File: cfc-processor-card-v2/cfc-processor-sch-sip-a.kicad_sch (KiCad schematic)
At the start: 27 parts, among them J4 Conn_01x04, Q6 MMBT2907, U7 OSD3358-1G-ISM, U8 SN74AUC1G07DCKR, U9 TLVH431

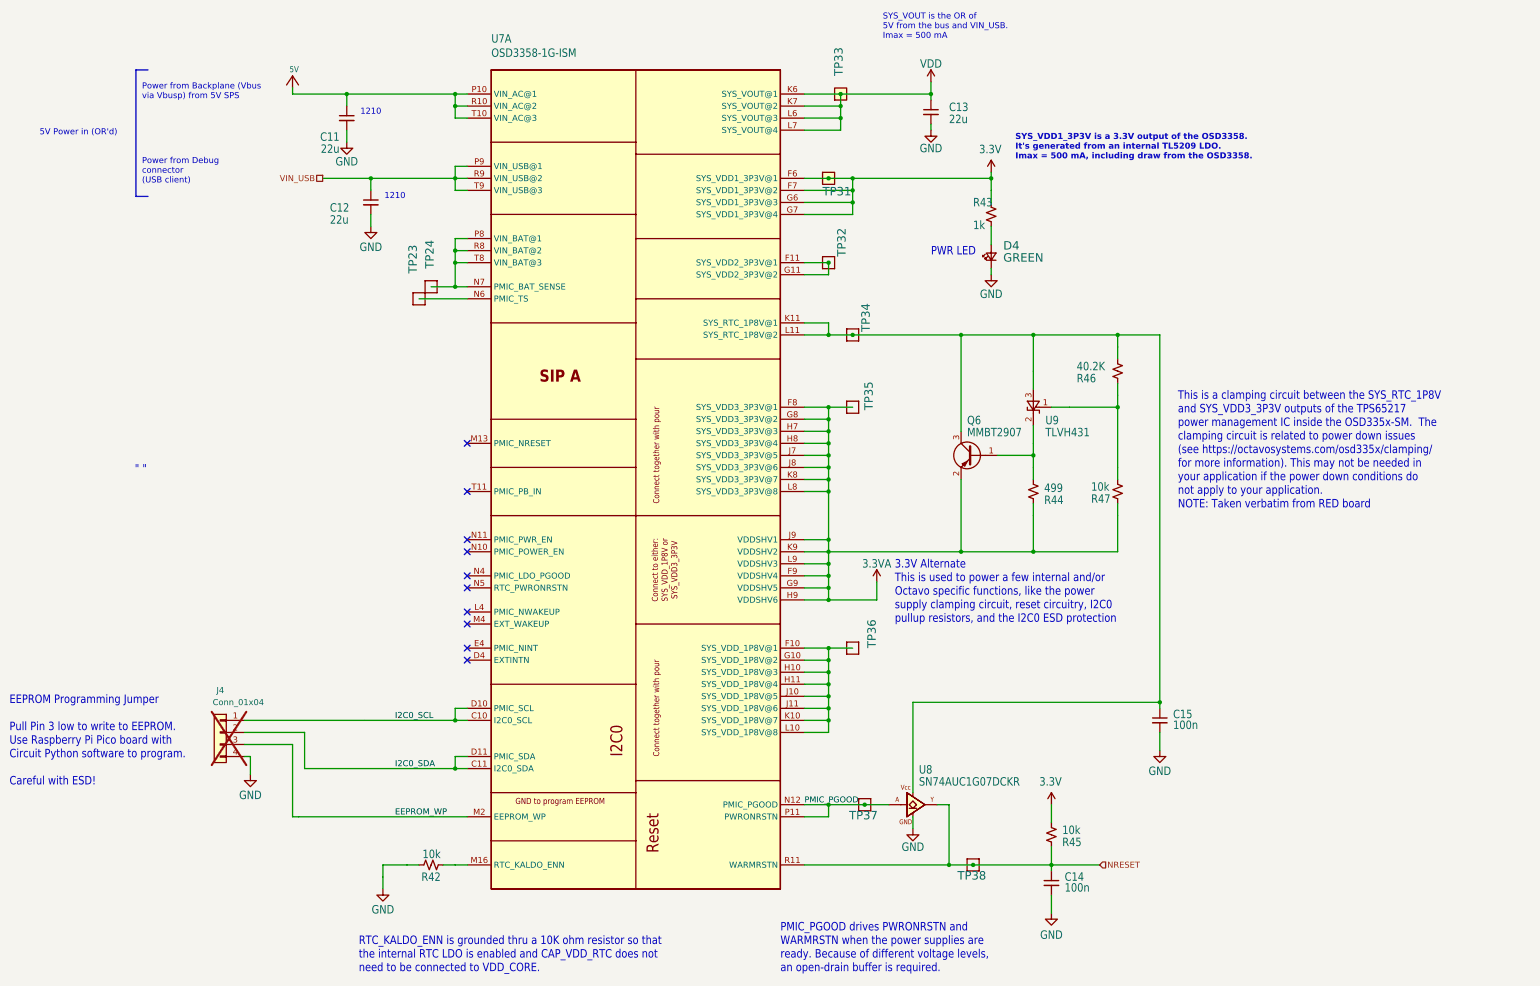
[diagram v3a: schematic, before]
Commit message: Update
Fixed a couple of library issues on testpoints and other misc components. Added Pull up resistors to 8 channel i2c ic
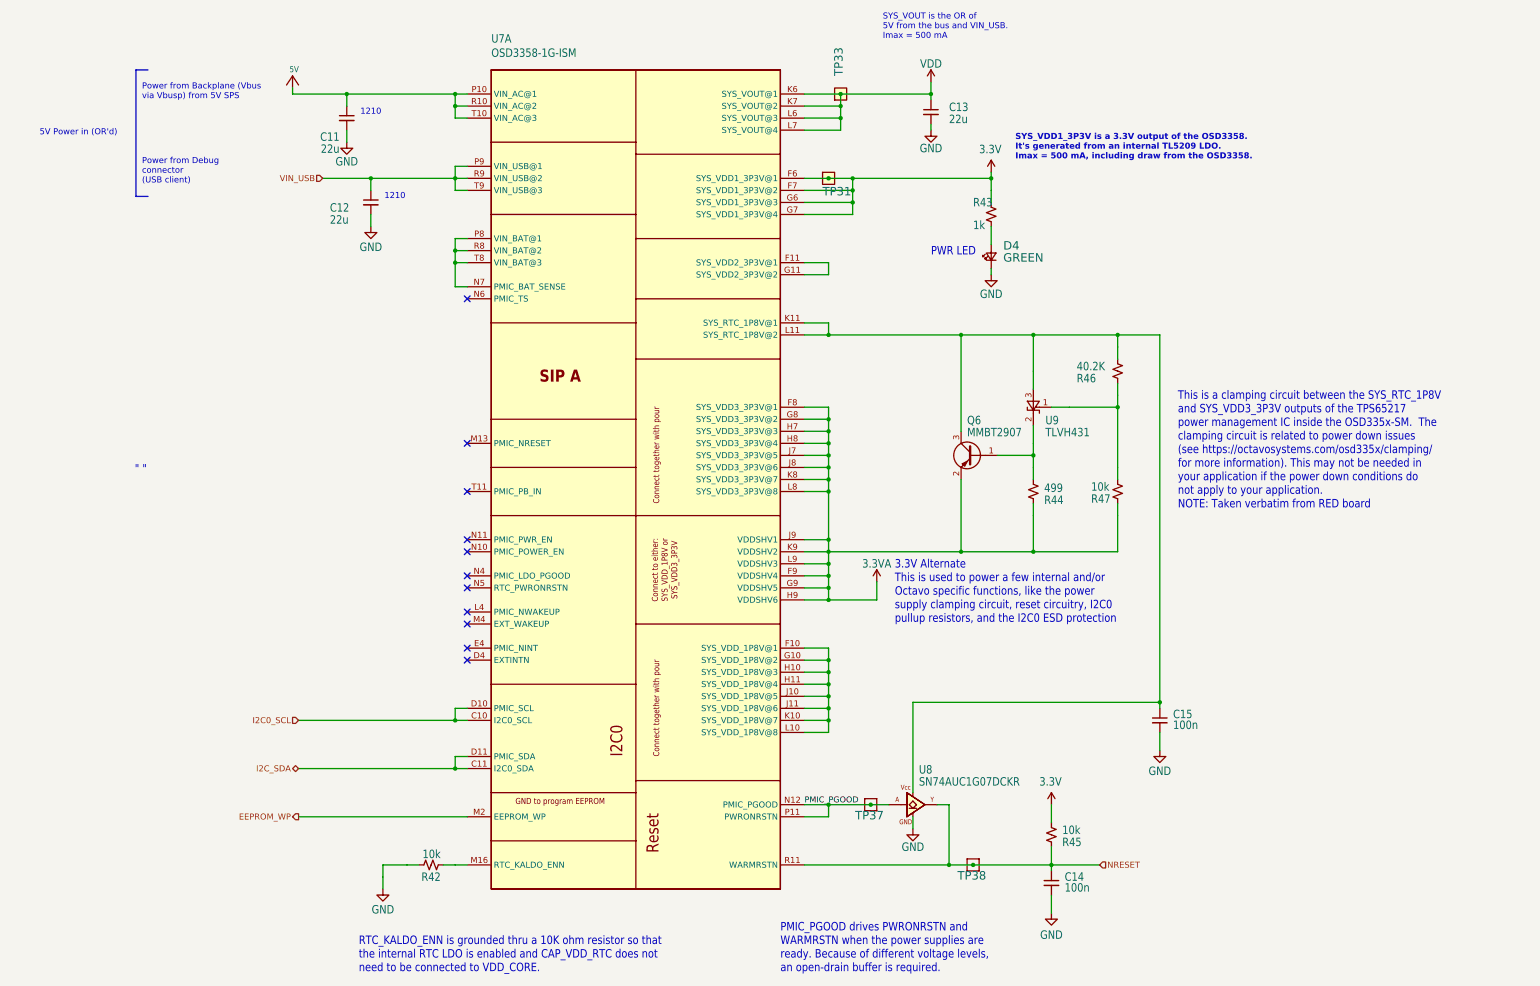
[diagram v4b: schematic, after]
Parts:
- removed J4: Conn_01x04, Connector_PinHeader_2.54mm:PinHeader_1x04_P2.54mm_Vertical, symbol Connector_Generic:Conn_01x04
- removed TP23, TP24, TP32, TP34, TP35, TP36: TEST-POINT3X4, oresat-misc:TestPoint_Pad_D1.0mm, symbol Oresat Misc:Test-Point-1mm-round
- TP31, TP33: symbol Oresat Misc:Test-Point-0.75mm-th -> oresat-misc:Test-Point-0.75mm-th
- TP37, TP38: symbol Oresat Misc:Test-Point-1mm-round -> oresat-misc:Test-Point-1mm-round
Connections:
- net I2C0_SDA renamed I2C_SDA
- no-connect marks 10 -> 11
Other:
- note removed: "EEPROM Programming Jumper Pull Pin 3 low to write to EEPROM. Use Raspberry Pi Pico board with Circuit Python software to program. Careful with ESD!"
- moved on the sheet: TP37
